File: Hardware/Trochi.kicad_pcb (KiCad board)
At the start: 2 copper layers, 54 parts, among them IC1 ICM-42688-P, J1 JST-SH, J2 JST-SH, J3 JST PH, J4 JST-SH, J5 JST-SH, J6 JST_SH, Q1 AO3401A, Q2 AO3400A, Q3 AO3400A, Q4 AO3400A, Q5 AO3400A, Q6 AO3400A, SW1 SW_SPDT, U1 ME6211C33M5, U3 YX-SMD5020

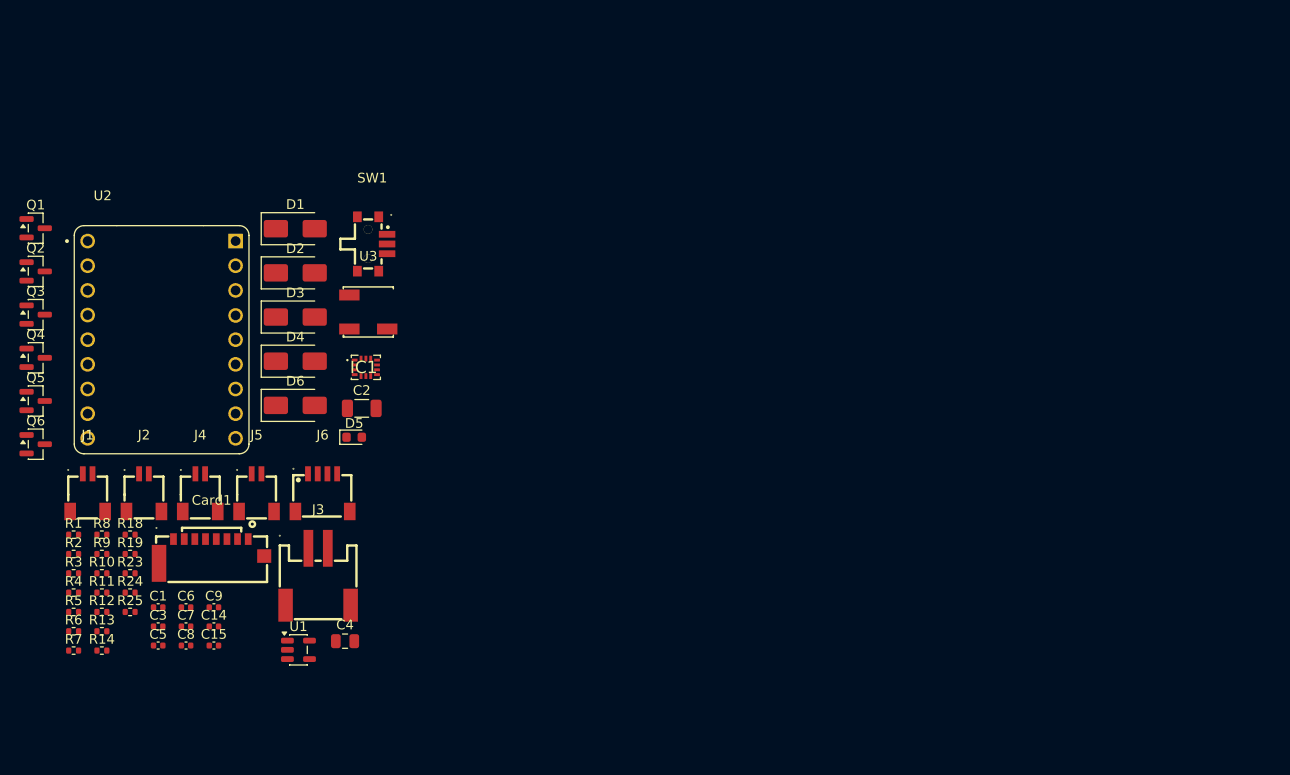
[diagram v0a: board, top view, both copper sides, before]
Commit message: feat: start bottom layer routing on PCB
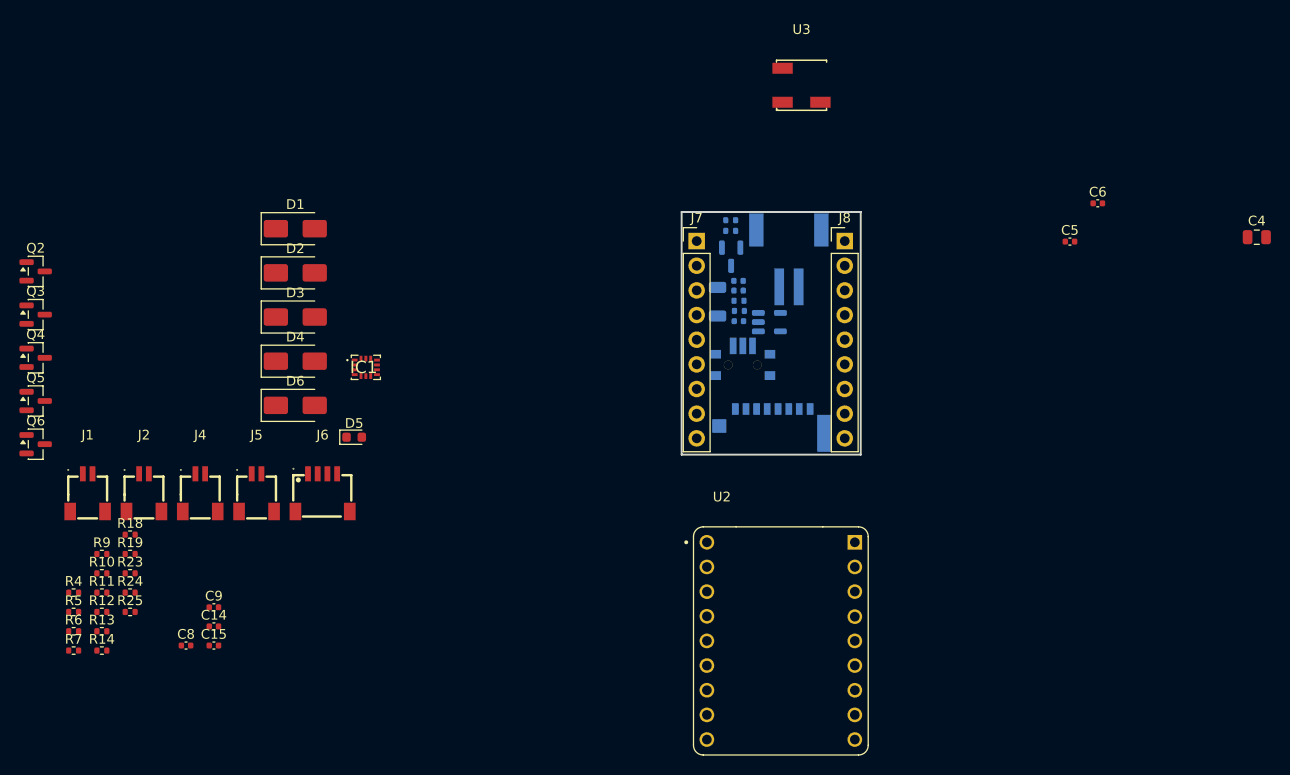
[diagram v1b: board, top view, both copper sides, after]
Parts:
- added J7: Conn_01x09, Connector_PinHeader_2.54mm:PinHeader_1x09_P2.54mm_Vertical, F.Cu at (174.1, 78.0)
- added J8: Conn_01x09, Connector_PinHeader_2.54mm:PinHeader_1x09_P2.54mm_Vertical, F.Cu at (189.3, 78.0)
- C1, C2, C3, C7, Card1, J3, Q1, R1, R2, R3, R8, SW1, U1: moved to B.Cu
- moved C4 102.7 mm to (231.8, 77.6)
- moved C6 102.7 mm to (215.4, 74.1)
- moved C5 102.7 mm to (212.5, 78.0)
- moved R2 75.9 mm to (177.6, 75.8), turned to 180 degrees
- moved R1 74.6 mm to (177.6, 77.0), turned to 180 degrees
- moved R3 74.1 mm to (178.4, 84.2)
- moved Q1 71.7 mm to (177.6, 79.6), turned to -90 degrees
- moved U2 70.9 mm to (182.7, 119.2)
- moved R8 69.6 mm to (178.4, 85.2), turned to 180 degrees
- moved C3 69.6 mm to (178.4, 82.1)
- moved C1 68.1 mm to (178.4, 83.1)
- moved C7 65.1 mm to (178.4, 86.2), turned to 180 degrees
- moved Card1 59.3 mm to (181.8, 96.5), turned to 180 degrees
- moved U1 59.1 mm to (181.5, 86.3)
- moved J3 58.5 mm to (183.6, 79.8)
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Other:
- board outline added: 18.4 x 25 mm

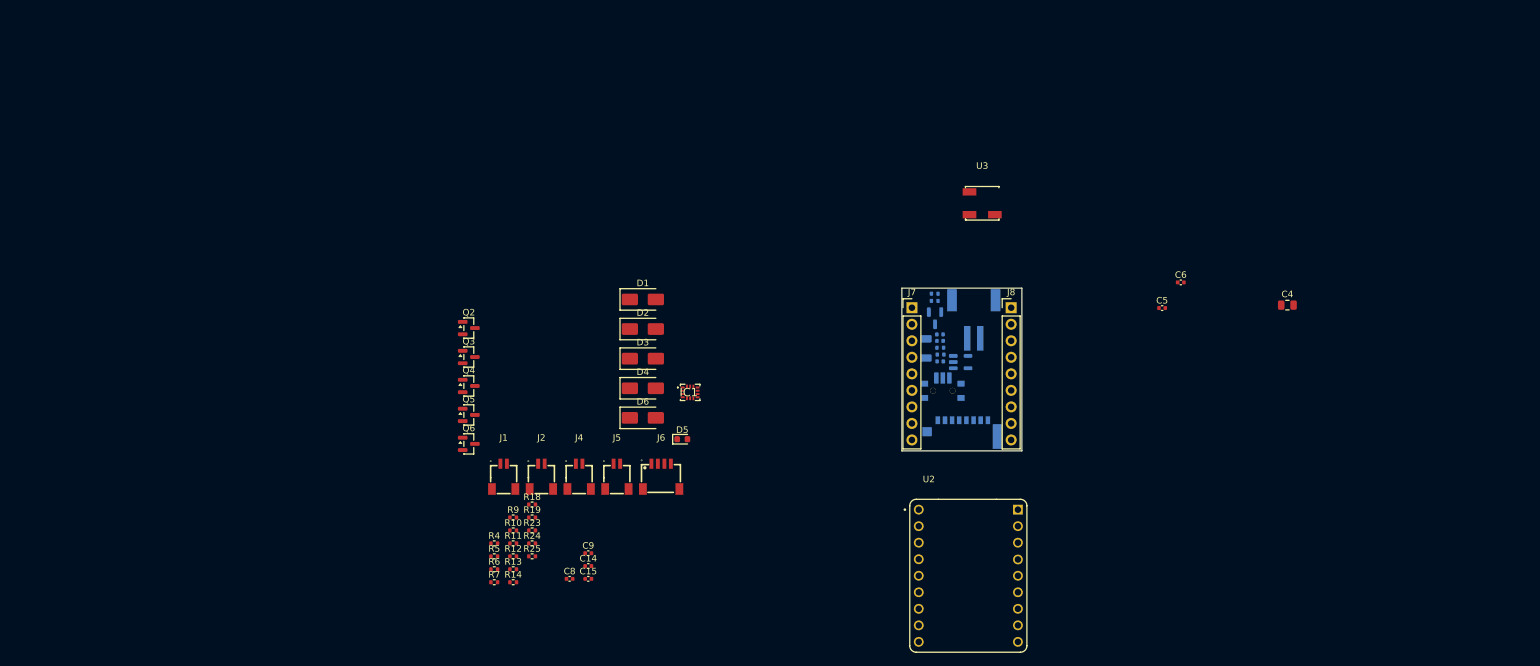
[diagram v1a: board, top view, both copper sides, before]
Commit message: feat: place bottom layer components on PCB
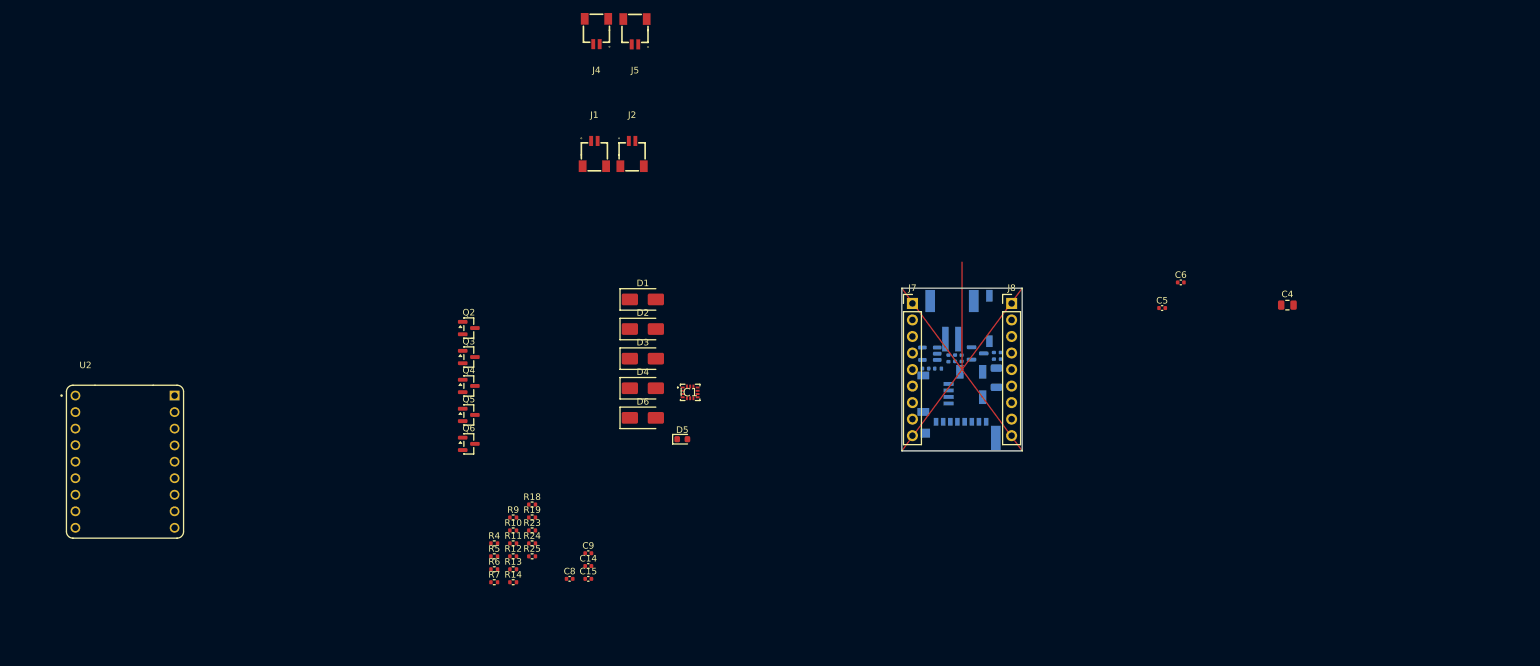
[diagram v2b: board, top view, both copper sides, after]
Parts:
- removed SW1: SW_SPDT, trochi_footprint:SW-TH_K3-1293S-E2
- added U4: ZX-1.27BM-1PSMD, trochi_footprint:SW-SMD_L5.4-W2.8-LS8.2, B.Cu at (185.9, 79.7)
- J6, U3: moved to B.Cu
- moved U2 130.8 mm to (53.1, 101.7)
- moved J4 68.4 mm to (125.6, 35.5), turned to 180 degrees
- moved J5 68.4 mm to (131.5, 35.6), turned to 180 degrees
- moved J2 51.5 mm to (131.1, 54.3)
- moved J1 51.5 mm to (125.2, 54.3)
- moved J6 44.1 mm to (177.7, 91.2), turned to 90 degrees
- moved U3 27.9 mm to (183.2, 89.8), turned to -90 degrees
- moved R1 13.2 mm to (187.7, 85.4), turned to -90 degrees
- moved R2 13.2 mm to (186.7, 85.4), turned to 90 degrees
- moved C2 11.7 mm to (187.0, 88.8)
- moved Q1 8.49 mm to (184.2, 85.0), turned to 0 degrees
- moved C3 4.95 mm to (181.7, 85.8), turned to -90 degrees
- moved U1 4.91 mm to (176.8, 85.1), turned to 180 degrees
- moved C1 3.52 mm to (180.7, 85.8), turned to -90 degrees
- moved J3 3.35 mm to (180.2, 79.9)
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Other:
- board size 18.4 x 25 mm -> 18.5 x 25 mm

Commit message: chore: update PCB from latest schematic changes
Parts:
- removed C14: 10µF, Capacitor_SMD:C_0402_1005Metric
- removed C15: 100nF, Capacitor_SMD:C_0402_1005Metric
- removed the J4 at (125.6, 35.5)
- removed the J5 at (131.5, 35.6)
- removed Q6: AO3400A, Package_TO_SOT_SMD:SOT-23
- removed R18: 100Ω, Resistor_SMD:R_0402_1005Metric
- removed R19, R23, R24, R25: 10KΩ, Resistor_SMD:R_0402_1005Metric
- removed U4: ZX-1.27BM-1PSMD, trochi_footprint:SW-SMD_L5.4-W2.8-LS8.2
- added C10: 100nF, Capacitor_SMD:C_0402_1005Metric, F.Cu at (124.9, 85.8)
- added C11: 100nF, Capacitor_SMD:C_0402_1005Metric, F.Cu at (127.7, 81.9)
- added C12: 10µF, Capacitor_SMD:C_0402_1005Metric, F.Cu at (127.7, 83.9)
- added C13: 100nF, Capacitor_SMD:C_0402_1005Metric, F.Cu at (127.7, 85.8)
- added J7: JST-SH, trochi_footprint:CONN-SMD_2P-P1.00_SM02B-SRSS-TB-LF-SN, F.Cu at (130.2, 65.6)
- added R15: 10KΩ, Resistor_SMD:R_0402_1005Metric, F.Cu at (127.8, 73.9)
- added R16: 100Ω, Resistor_SMD:R_0402_1005Metric, F.Cu at (127.8, 75.9)
- added R17: 10KΩ, Resistor_SMD:R_0402_1005Metric, F.Cu at (127.8, 77.9)
- C1, C7, R1, U1, U3: moved to F.Cu
- C2: value 100µF -> 22µF; footprint Capacitor_SMD:C_1206_3216Metric -> Capacitor_SMD:C_0603_1608Metric; moved to F.Cu
- C3: value 10µF -> 22µF; footprint Capacitor_SMD:C_0402_1005Metric -> Capacitor_SMD:C_0603_1608Metric; moved to F.Cu
- C4: footprint Capacitor_SMD:C_0805_2012Metric -> Capacitor_SMD:C_0603_1608Metric
- C5: value 100nF -> 10µF
- C6: value 100nF -> 22µF; footprint Capacitor_SMD:C_0402_1005Metric -> Capacitor_SMD:C_0805_2012Metric
- D1, D2, D3, D4, D6: value SS14 -> 1N5819W; footprint Diode_SMD:D_SMA -> Diode_SMD:D_SOD-123
- J6: value JST_SH -> JST-SH; footprint trochi_footprint:CONN-SMD_4P-P1.00_SM04B-SRSS-TB-LF-SN -> trochi_footprint:CONN-SMD_2P-P1.00_SM02B-SRSS-TB-LF-SN; moved to F.Cu
- Q1: value AO3401A -> AO3400A; moved to F.Cu
- R10, R4, R9: value 100Ω -> 10KΩ
- R11: value 10KΩ -> 1KΩ
- R13: value 1KΩ -> 10KΩ
- R2: value 1KΩ -> 100Ω; moved to F.Cu
- R3, R8: value 100KΩ -> 100Ω; moved to F.Cu
- R5: value 100Ω -> 10Ω
- R6: value 10KΩ -> 100KΩ
- R7: value 10Ω -> 100Ω
- moved C4 101.0 mm to (131.2, 87.2)
- moved C6 93.7 mm to (122.8, 88.3)
- moved C5 90.7 mm to (122.0, 83.9)
- moved Q1 73.2 mm to (112.3, 71.2)
- moved R1 67.5 mm to (122.0, 70.0), turned to 0 degrees
- moved R2 66.0 mm to (122.0, 72.0), turned to 0 degrees
- moved U1 59.5 mm to (117.3, 88.1), turned to 0 degrees
- moved J6 59.2 mm to (124.4, 65.6), turned to 0 degrees
- moved R3 58.8 mm to (122.0, 73.9), turned to 0 degrees
- moved C1 58.8 mm to (122.0, 81.9), turned to 0 degrees
- moved C2 56.3 mm to (131.2, 82.2), turned to 0 degrees
- moved R8 55.3 mm to (124.9, 72.0), turned to 0 degrees
- moved C7 54.2 mm to (122.0, 85.8), turned to 0 degrees
- moved U3 53.4 mm to (132.8, 72.1), turned to 0 degrees
- moved R7 52.4 mm to (124.9, 70.0)
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- renumbered J7 to J4, J8 to J5
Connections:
- C4 pad 1: +3.3V -> /VBAT
- C5 pad 1: +3.3V -> /VBAT
- C7 pad 1: VBAT_SENSE -> +3.3V
- C9 pad 1: +3.3V -> VBAT_SENSE
- J3 pad 2: Net-(J3-Pin_2) -> /VBAT
- J6 pad 1: +3.3V -> Net-(D3-A)
- J6 pad 2: GND -> /VBAT
- Q1 pad 2: Net-(J3-Pin_2) -> GND
- Q1 pad 3: /VBAT -> Net-(D1-A)
- Q2 pad 3: Net-(D1-A) -> Net-(D2-A)
- Q3 pad 3: Net-(D2-A) -> Net-(D3-A)
- Q4 pad 3: Net-(D3-A) -> Net-(D4-A)
- Q5 pad 3: Net-(D4-A) -> Net-(D6-A)
- R1 pad 1: Net-(J3-Pin_2) -> /VBAT
- R1 pad 2: Net-(Q1-G) -> VBAT_SENSE
- R10 pad 1: PWM_M4 -> Net-(Q4-G)
- R10 pad 2: Net-(Q5-G) -> GND
- R11 pad 1: Net-(Q4-G) -> Net-(D5-K)
- R12 pad 1: Net-(Q5-G) -> +3.3V
- R12 pad 2: GND -> CS_IMU
- R13 pad 1: Net-(D5-K) -> +3.3V
- R13 pad 2: GND -> SPI_MOSI
- R14 pad 2: CS_IMU -> CS_SD
- R2 pad 1: Net-(Q1-G) -> PWM_M1
- R2 pad 2: Net-(R2-Pad2) -> Net-(Q1-G)
- R3 pad 1: /VBAT -> PWM_M2
- R3 pad 2: VBAT_SENSE -> Net-(Q2-G)
- R4 pad 1: PWM_M1 -> Net-(Q1-G)
- R4 pad 2: Net-(Q2-G) -> GND
- R5 pad 1: PWM_M2 -> Net-(Q2-G)
- R5 pad 2: Net-(Q3-G) -> GND
- R6 pad 1: Net-(Q2-G) -> VBAT_SENSE
- R7 pad 1: Net-(Q3-G) -> PWM_M3
- R7 pad 2: GND -> Net-(Q3-G)
- R8 pad 1: VBAT_SENSE -> PWM_M4
- R8 pad 2: GND -> Net-(Q4-G)
- R9 pad 1: PWM_M3 -> Net-(Q3-G)
- R9 pad 2: Net-(Q4-G) -> GND
- U2 pad RX: RC_TX -> unconnected-(U2-PadRX)
- U2 pad TX: RC_RX -> unconnected-(U2-PadTX)

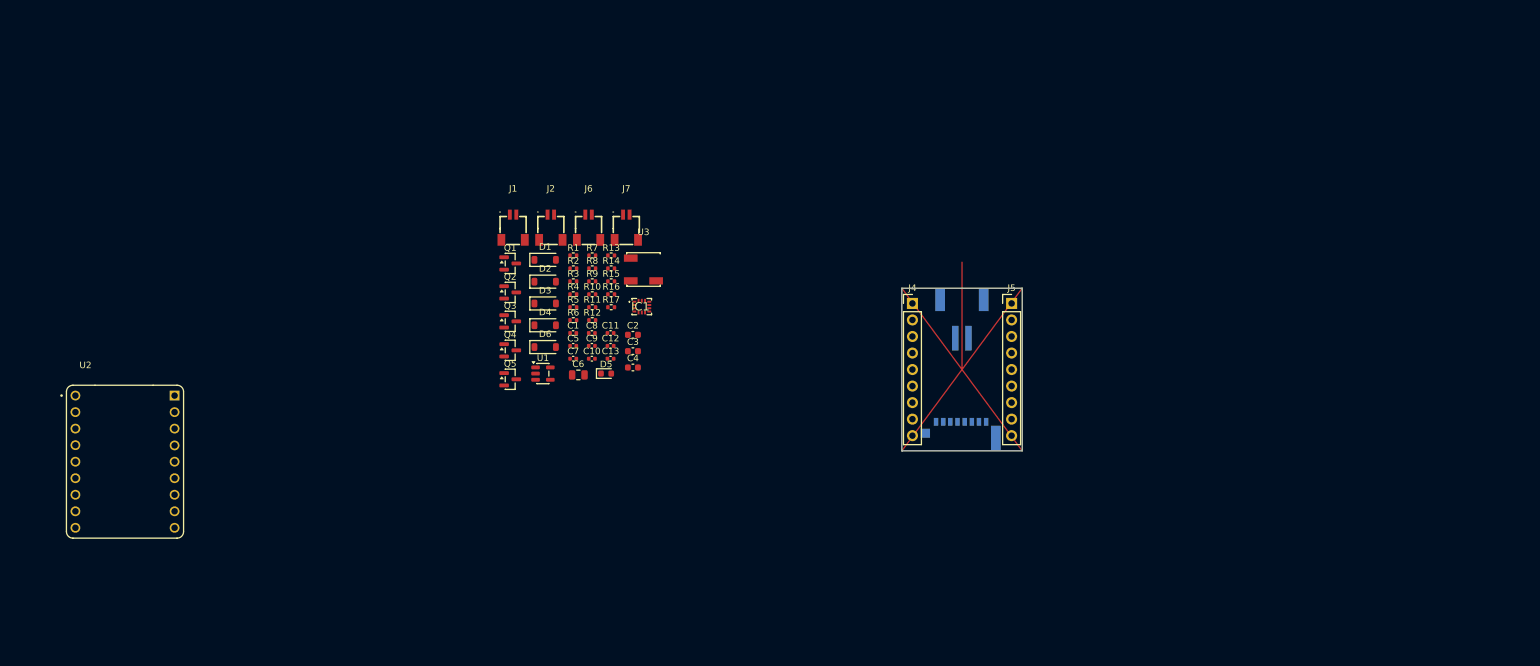
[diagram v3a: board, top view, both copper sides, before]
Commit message: chore: finalize bottom layer component placement
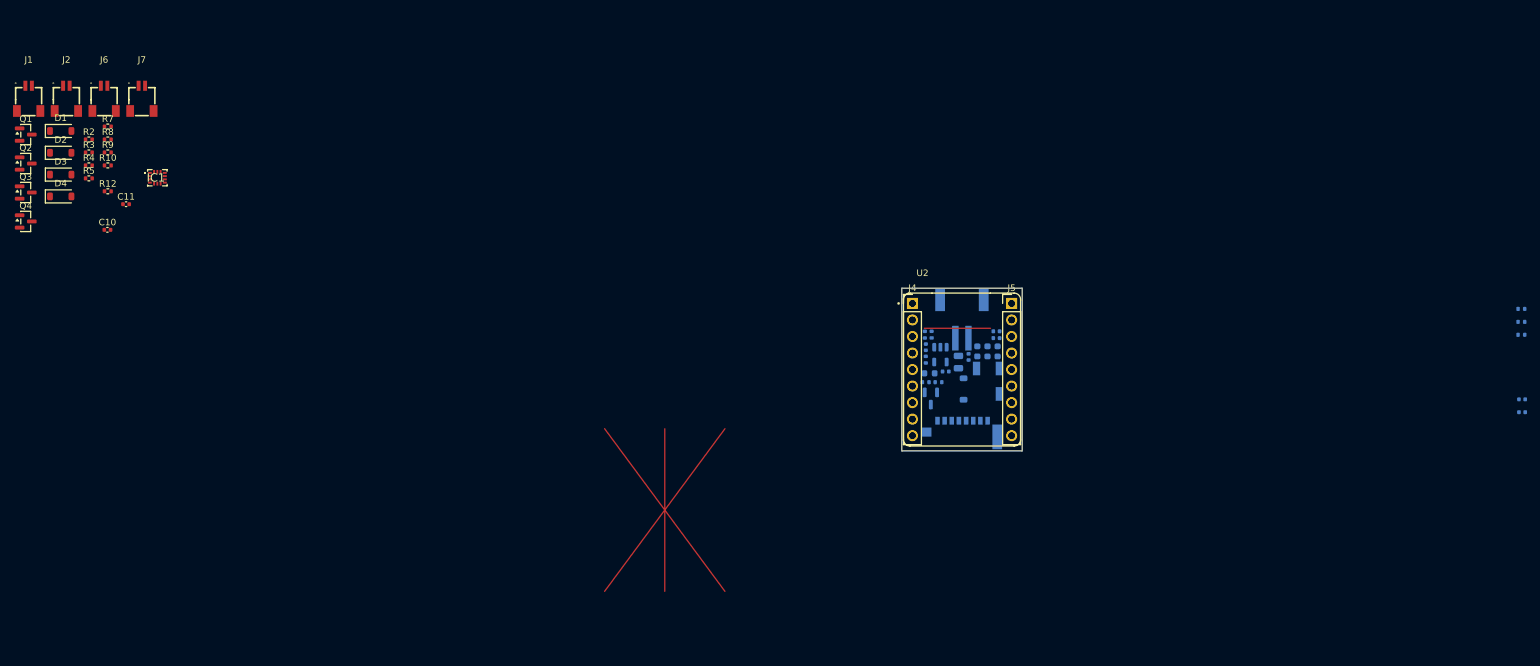
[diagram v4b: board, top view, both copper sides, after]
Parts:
- C1, C12, C13, C2, C3, C4, C5, C6, C7, C8, C9, D5, D6, Q5, R1, R11, R13, R14, R15, R16, R17, R6, U1, U3: moved to B.Cu
- moved C12 140.3 mm to (267.8, 92.1), turned to 180 degrees
- moved C13 140.3 mm to (267.8, 94.0), turned to 180 degrees
- moved R13 140.1 mm to (267.7, 78.2), turned to 180 degrees
- moved R14 140.1 mm to (267.7, 80.2), turned to 180 degrees
- moved R15 140.1 mm to (267.7, 82.2), turned to 180 degrees
- moved U2 129.4 mm to (181.8, 87.5)
- moved J1 77.0 mm to (38.3, 45.8)
- moved J2 77.0 mm to (44.1, 45.8)
- moved J6 77.0 mm to (49.9, 45.8)
- moved D2 77.0 mm to (43.2, 54.2)
- moved J7 77.0 mm to (55.7, 45.8)
- moved Q4 77.0 mm to (37.9, 64.7)
- moved R12 77.0 mm to (50.5, 60.1)
- moved R7 77.0 mm to (50.5, 50.2)
- moved C11 77.0 mm to (53.3, 62.1)
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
